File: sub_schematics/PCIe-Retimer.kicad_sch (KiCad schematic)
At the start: 1 part, among them U1 DS160PT801ACBR

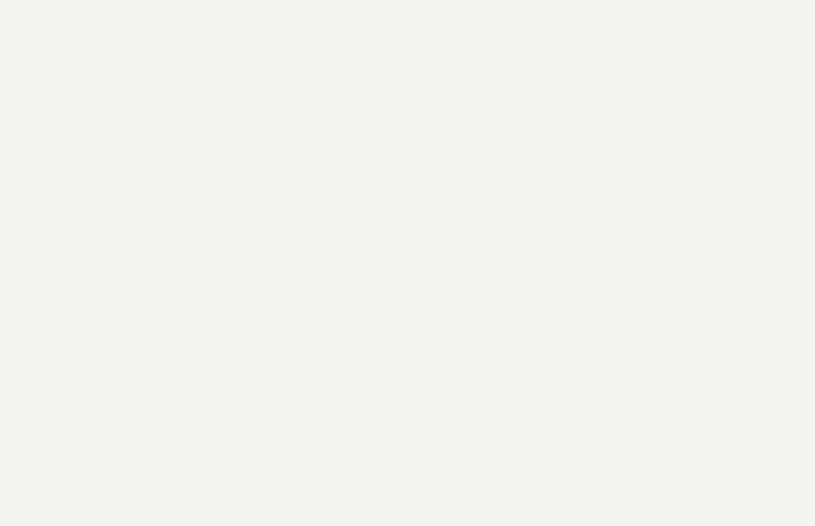
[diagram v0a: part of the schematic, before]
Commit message: moved schematics
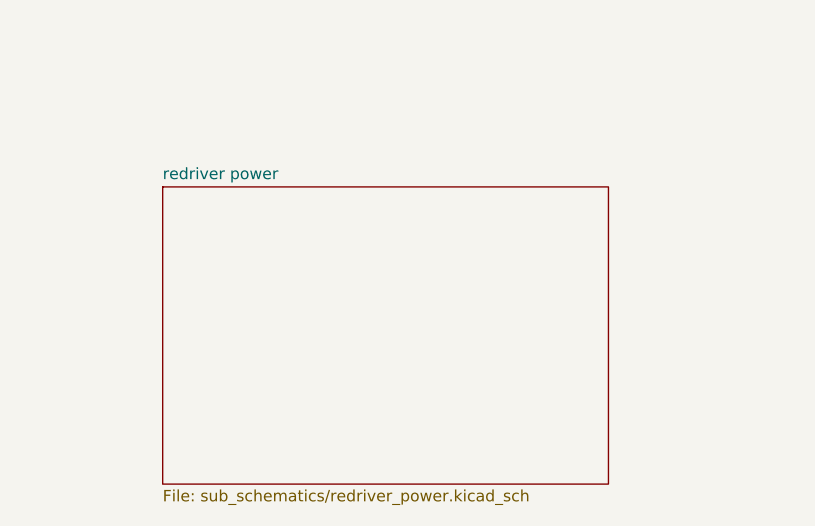
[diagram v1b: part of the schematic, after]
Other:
- added sheet redriver power (sub_schematics/redriver_power.kicad_sch)
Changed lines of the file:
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@@
+		)
+	)
+	(sheet
+		(at 165.1 267.97)
+		(size 49.53 33.02)
+		(exclude_from_sim no)
+		(in_bom yes)
+		(on_board yes)
+		(dnp no)
+		(fields_autoplaced yes)
+		(stroke
+			(width 0.1524)
+			(type solid)
+		)
+		(fill
+			(color 0 0 0 0)
+		)
+		(property "Sheetname" "redriver power"
+			(at 165.1 267.2584 0)
+			(show_name no)
+			(do_not_autoplace no)
+			(effects
+				(font
+					(size 1.27 1.27)
+				)
+				(justify left bottom)
+			)
+		)
+		(property "Sheetfile" "sub_schematics/redriver_power.kicad_sch"
+			(at 165.1 301.5746 0)
+			(show_name no)
+			(do_not_autoplace no)
+			(effects
+				(font
+					(size 1.27 1.27)
+				)
+				(justify left top)
+			)
+		)
+		(instances
+			(project "fw16_MCIO8i"
+				(path "/50f5fd03-67f8-43d1-8bfe-dca2cf908bf0/b129293c-459e-48f0-b955-fe94d8ad35a8"
+					(page "4")
+				)
+			)
 		)
 	)
